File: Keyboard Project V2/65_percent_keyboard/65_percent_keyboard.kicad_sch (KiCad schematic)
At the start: 12 parts, among them SW1 SW_Push, U1 ATmega32A-P, U2 FT232RL, Y1 16MHz

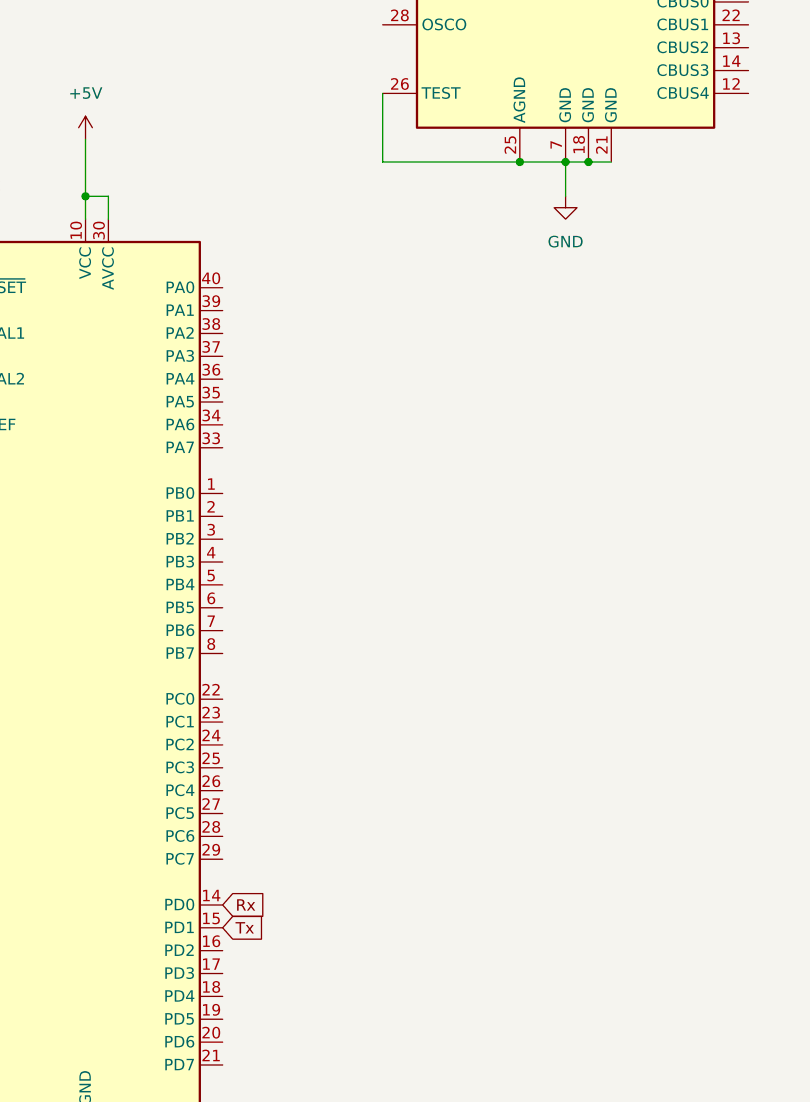
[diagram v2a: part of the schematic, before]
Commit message: fixed the Rx/Tx wire
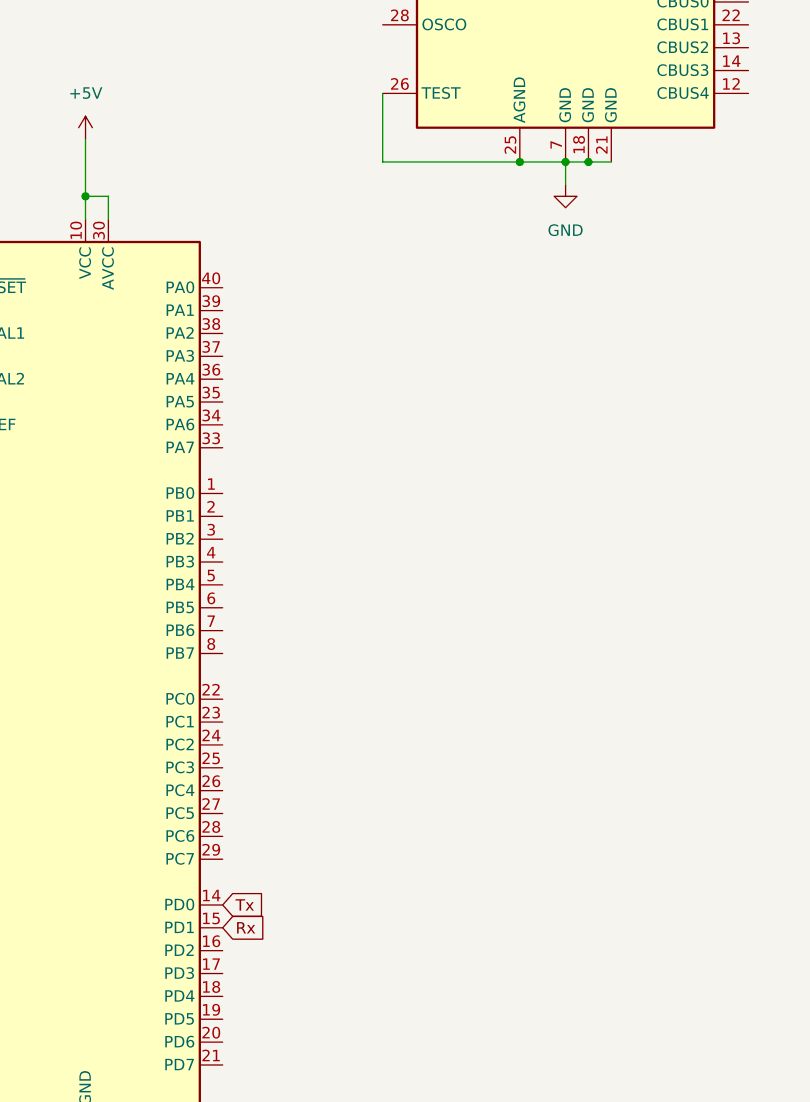
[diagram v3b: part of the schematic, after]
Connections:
- net Rx: now also U1.15 (PD1); no longer U1.14 (PD0)
- net Tx: now also U1.14 (PD0); no longer U1.15 (PD1)
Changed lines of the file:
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@@
+    (stroke (width 0) (type default))
+  )
+  (wire (pts (xy 121.92 80.01) (xy 121.92 82.55))
     (stroke (width 0) (type default))
   )
@@
   )
   (wire (pts (xy 33.02 22.86) (xy 41.91 22.86))
-    (stroke (width 0) (type default))
-  )
-  (wire (pts (xy 121.92 80.01) (xy 121.92 83.82))
     (stroke (width 0) (type default))
   )
@@
     )
   )
-  (global_label "Rx" (shape input) (at 83.82 162.56 0) (fields_autoplaced)
-    (effects (font (size 1.27 1.27)) (justify left))
-    (property "Intersheetrefs" "${INTERSHEET_REFS}" (at 89.0239 162.56 0)
-      (effects (font (size 1.27 1.27)) (justify left) hide)
-    )
-  )
-  (global_label "Tx" (shape input) (at 83.82 165.1 0) (fields_autoplaced)
-    (effects (font (size 1.27 1.27)) (justify left))
-    (property "Intersheetrefs" "${INTERSHEET_REFS}" (at 88.7215 165.1 0)
+  (global_label "Rx" (shape input) (at 83.82 165.1 0) (fields_autoplaced)
+    (effects (font (size 1.27 1.27)) (justify left))
+    (property "Intersheetrefs" "${INTERSHEET_REFS}" (at 89.0239 165.1 0)
+      (effects (font (size 1.27 1.27)) (justify left) hide)
+    )
+  )
+  (global_label "Tx" (shape input) (at 83.82 162.56 0) (fields_autoplaced)
+    (effects (font (size 1.27 1.27)) (justify left))
+    (property "Intersheetrefs" "${INTERSHEET_REFS}" (at 88.7215 162.56 0)
       (effects (font (size 1.27 1.27)) (justify left) hide)
     )
@@
     )
   )
-  (symbol (lib_id "power:GND") (at 121.92 83.82 0) (unit 1)
-    (in_bom yes) (on_board yes) (dnp no) (fields_autoplaced)
-    (property "Reference" "#PWR08" (at 121.92 90.17 0)
-      (effects (font (size 1.27 1.27)) hide)
-    )
-    (property "Value" "GND" (at 121.92 88.9 0)
-      (effects (font (size 1.27 1.27)))
-    )
-    (property "Footprint" "" (at 121.92 83.82 0)
-      (effects (font (size 1.27 1.27)) hide)
-    )
-    (property "Datasheet" "" (at 121.92 83.82 0)
-      (effects (font (size 1.27 1.27)) hide)
-    )
+  (symbol (lib_id "power:GND") (at 121.92 82.55 0) (unit 1)
+    (in_bom yes) (on_board yes) (dnp no) (fields_autoplaced)
+    (property "Reference" "#PWR08" (at 121.92 88.9 0)
+      (effects (font (size 1.27 1.27)) hide)
+    )
+    (property "Value" "GND" (at 121.92 87.63 0)
+      (effects (font (size 1.27 1.27)))
+    )
+    (property "Footprint" "" (at 121.92 82.55 0)
+      (effects (font (size 1.27 1.27)) hide)
+    )
+    (property "Datasheet" "" (at 121.92 82.55 0)
+      (effects (font (size 1.27 1.27)) hide)
+    )
